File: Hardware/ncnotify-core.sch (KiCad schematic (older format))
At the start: 44 parts, among them J1 BNC5-J-P-GN-RA-BH2D, J2 Conn_ARM_JTAG_SWD_10, J3 USB4110-GF-A, Q1 NX3008NBKS, SW1 SW_Push, SW2 SW_Push, U1 STM32L422CBT6, U2 TLV71333PDBV, U3 USBLC6-2SC6, U4 USBLC6-2SC6, X1 SMTU1632-LF, Y1 Q13FC1350000400

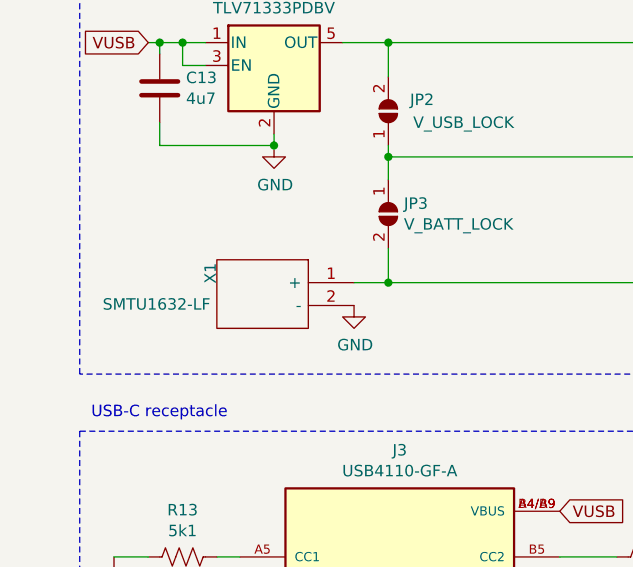
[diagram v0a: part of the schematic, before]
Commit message: sizeup batt to 2032 for current limit; re-place to fit
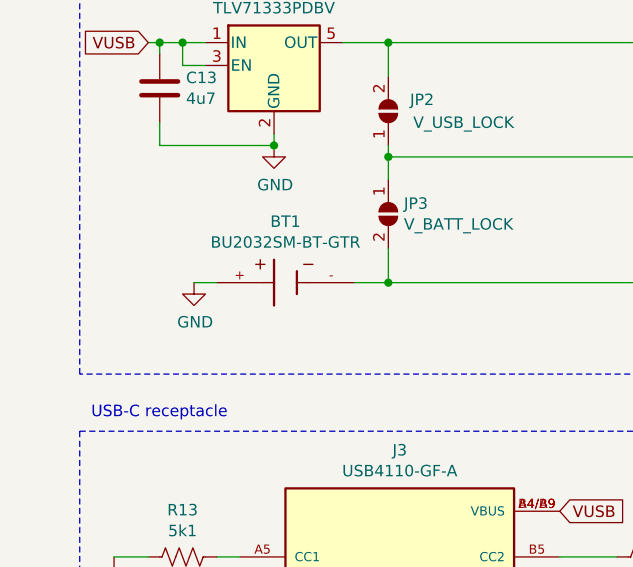
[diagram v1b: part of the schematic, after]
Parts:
- removed X1: SMTU1632-LF, SamacSys_Parts:SMTU1632LF, symbol SamacSys_Parts:SMTU1632-LF
- added BT1: BU2032SM-BT-GTR, BAT_BU2032SM-BT-GTR, symbol BU2032SM-BT-GTR:BU2032SM-BT-GTR
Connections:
- net GND: now also BT1.+
- net VBAT: now also BT1.-
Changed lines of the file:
@@
 Text Notes 3450 600  2    50   ~ 0
 Ext. crystal (LSE)
-$Comp
-L SamacSys_Parts:SMTU1632-LF X1
-U 1 1 5FA9A6FE
-P 1850 5400
-F 0 "X1" V 2478 5396 50  0000 L CNN
-F 1 "SMTU1632-LF" H 2478 5305 50  0000 L CNN
-F 2 "SamacSys_Parts:SMTU1632LF" H 2500 5500 50  0001 L CNN
-F 3 "https://componentsearchengine.com/Datasheets/1/SMTU1632-LF.pdf" H 2500 5400 50  0001 L CNN
-F 4 "Coin Cell Battery Holders SFC MNT FOR CR1632" H 2500 5300 50  0001 L CNN "Description"
-F 5 "5.4" H 2500 5200 50  0001 L CNN "Height"
-F 6 "614-SMTU1632-LF" H 2500 5100 50  0001 L CNN "Mouser Part Number"
-F 7 "https://www.mouser.co.uk/ProductDetail/Renata/SMTU1632-LF?qs=WWgnj3qycfliEHm3l%252BmM0A%3D%3D" H 2500 5000 50  0001 L CNN "Mouser Price/Stock"
-F 8 "RENATA" H 2500 4900 50  0001 L CNN "Manufacturer_Name"
-F 9 "SMTU1632-LF" H 2500 4800 50  0001 L CNN "Manufacturer_Part_Number"
-F 10 "" H 1850 5400 50  0001 C CNN "LCSC Part #"
-	1    1850 5400
-	-1   0    0    -1
-$EndComp
 Text Notes 750  600  0    50   ~ 0
 BNC sense connector
@@
 L power:GND #PWR023
 U 1 1 5FACABCF
-P 1850 5500
-F 0 "#PWR023" H 1850 5250 50  0001 C CNN
-F 1 "GND" H 1855 5327 50  0000 C CNN
-F 2 "" H 1850 5500 50  0001 C CNN
-F 3 "" H 1850 5500 50  0001 C CNN
-	1    1850 5500
+P 1150 5400
+F 0 "#PWR023" H 1150 5150 50  0001 C CNN
+F 1 "GND" H 1155 5227 50  0000 C CNN
+F 2 "" H 1150 5400 50  0001 C CNN
+F 3 "" H 1150 5400 50  0001 C CNN
+	1    1150 5400
 	1    0    0    -1
 $EndComp
@@
 	-1   0    0    1
 $EndComp
+$Comp
+L BU2032SM-BT-GTR:BU2032SM-BT-GTR BT1
+U 1 1 5FDB3DD9
+P 1550 5400
+F 0 "BT1" H 1550 5667 50  0000 C CNN
+F 1 "BU2032SM-BT-GTR" H 1550 5576 50  0000 C CNN
+F 2 "BAT_BU2032SM-BT-GTR" H 1550 5400 50  0001 L BNN
+F 3 "" H 1550 5400 50  0001 L BNN
+F 4 "BU2032SM-HD-G" H 1550 5400 50  0001 L BNN "MP"
+F 5 "MPD _Memory" H 1550 5400 50  0001 L BNN "MF"
+F 6 "None" H 1550 5400 50  0001 L BNN "PACKAGE"
+F 7 "None" H 1550 5400 50  0001 L BNN "PRICE"
+F 8 "F" H 1550 5400 50  0001 L BNN "PARTREV"
+F 9 "5.20mm" H 1550 5400 50  0001 L BNN "MAXIMUM_PACKAGE_HEIGHT"
+F 10 "Unavailable" H 1550 5400 50  0001 L BNN "AVAILABILITY"
+F 11 "BATTERY HOLDER COIN 20MM SMD" H 1550 5400 50  0001 L BNN "DESCRIPTION"
+	1    1550 5400
+	1    0    0    -1
+$EndComp
+Wire Wire Line
+	1150 5400 1250 5400
 $EndSCHEMATC

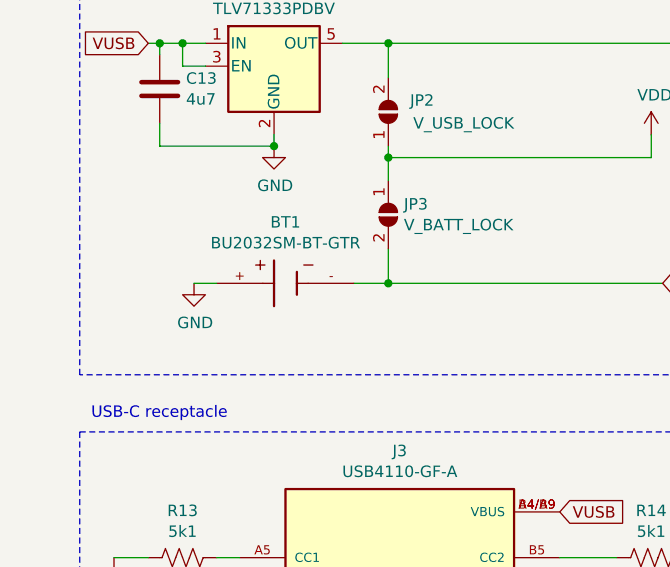
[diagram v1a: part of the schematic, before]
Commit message: Resolve TH conflicts; add 3d models
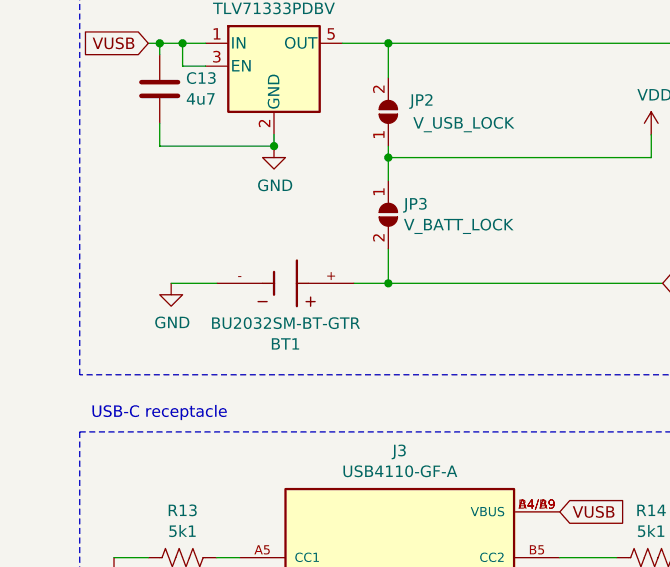
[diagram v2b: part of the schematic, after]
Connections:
- net GND: now also BT1.-; no longer BT1.+
- net VBAT: now also BT1.+; no longer BT1.-
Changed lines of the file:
@@
 L power:GND #PWR023
 U 1 1 5FACABCF
-P 1150 5400
-F 0 "#PWR023" H 1150 5150 50  0001 C CNN
-F 1 "GND" H 1155 5227 50  0000 C CNN
-F 2 "" H 1150 5400 50  0001 C CNN
-F 3 "" H 1150 5400 50  0001 C CNN
-	1    1150 5400
+P 1050 5400
+F 0 "#PWR023" H 1050 5150 50  0001 C CNN
+F 1 "GND" H 1055 5227 50  0000 C CNN
+F 2 "" H 1050 5400 50  0001 C CNN
+F 3 "" H 1050 5400 50  0001 C CNN
+	1    1050 5400
 	1    0    0    -1
 $EndComp
@@
 F 11 "BATTERY HOLDER COIN 20MM SMD" H 1550 5400 50  0001 L BNN "DESCRIPTION"
 	1    1550 5400
-	1    0    0    -1
-$EndComp
-Wire Wire Line
-	1150 5400 1250 5400
+	-1   0    0    1
+$EndComp
+Wire Wire Line
+	1050 5400 1250 5400
 $EndSCHEMATC

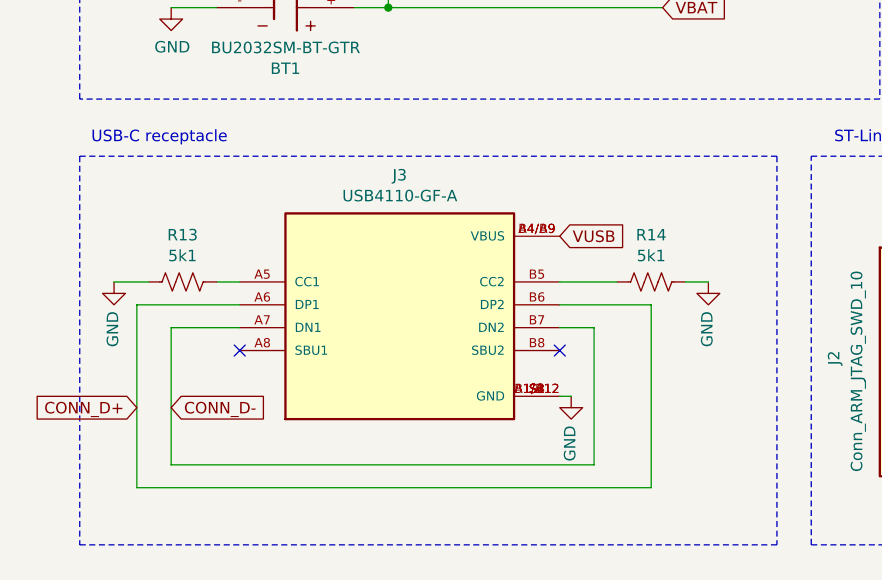
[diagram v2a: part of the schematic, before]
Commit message: micro-usb connector
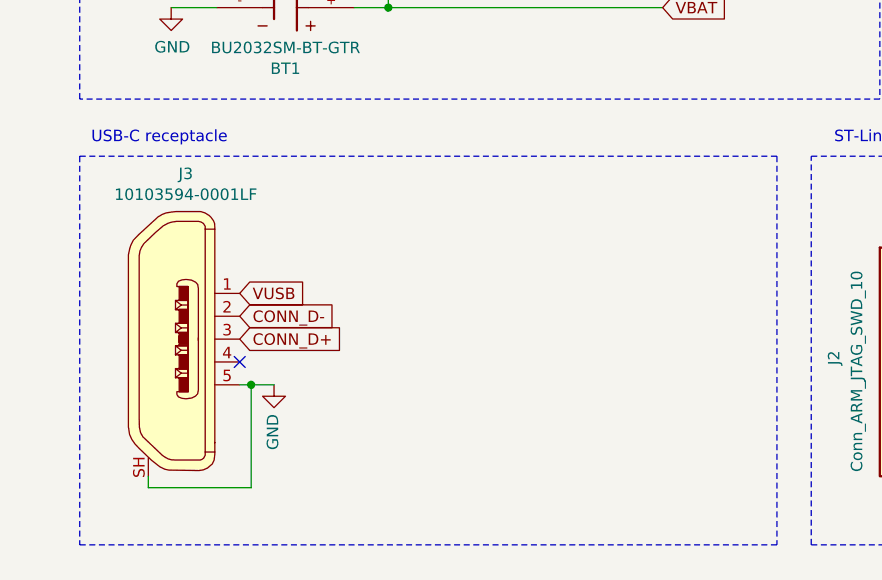
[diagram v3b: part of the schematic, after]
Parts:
- removed J3: USB4110-GF-A, libs:GCT_USB4110-GF-A, symbol USB4110-GF-A:USB4110-GF-A
- removed R13, R14: 5k1, Resistor_SMD:R_0402_1005Metric, symbol Device:R_US
- added J3: 10103594-0001LF, digikey-footprints:USB_Micro_B_Female_10103594-0001LF, symbol dk_USB-DVI-HDMI-Connectors:10103594-0001LF
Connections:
- net CONN_D+: now also J3.3
- net CONN_D-: now also J3.2
- net GND: now also J3.5, J3.SH
- net VUSB: now also J3.1
- no-connect marks 26 -> 25
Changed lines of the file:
@@
 Text Notes 750  600  0    50   ~ 0
 BNC sense connector
-$Comp
-L USB4110-GF-A:USB4110-GF-A J3
-U 1 1 5FA9CA6A
-P 2050 6700
-F 0 "J3" H 2050 7267 50  0000 C CNN
-F 1 "USB4110-GF-A" H 2050 7176 50  0000 C CNN
-F 2 "libs:GCT_USB4110-GF-A" H 2050 6700 50  0001 L BNN
-F 3 "" H 2050 6700 50  0001 L BNN
-F 4 "3.26 mm" H 2050 6700 50  0001 L BNN "MAXIMUM_PACKAGE_HEIGHT"
-F 5 "A" H 2050 6700 50  0001 L BNN "PARTREV"
-F 6 "GCT" H 2050 6700 50  0001 L BNN "MANUFACTURER"
-F 7 "Manufacturer Recommendations" H 2050 6700 50  0001 L BNN "STANDARD"
-F 8 "" H 2050 6700 50  0001 C CNN "LCSC Part #"
-	1    2050 6700
-	1    0    0    -1
-$EndComp
-Text GLabel 900  7150 0    50   Input ~ 0
+Text GLabel 1350 6850 2    50   Input ~ 0
 CONN_D+
-Text GLabel 1050 7150 2    50   Input ~ 0
+Text GLabel 1350 6750 2    50   Input ~ 0
 CONN_D-
-Wire Wire Line
-	1350 6800 1050 6800
-Wire Wire Line
-	1050 7400 2900 7400
-Wire Wire Line
-	900  7500 900  6700
-Wire Wire Line
-	900  6700 1350 6700
-Text GLabel 2750 6400 2    50   Input ~ 0
+Text GLabel 1350 6650 2    50   Input ~ 0
 VUSB
 Wire Notes Line
@@
 Wire Notes Line
 	4950 650  4950 2050
-Wire Wire Line
-	1050 6800 1050 7400
-$Comp
-L Device:R_US R14
-U 1 1 5FAA6CB5
-P 3150 6600
-F 0 "R14" V 2945 6600 50  0000 C CNN
-F 1 "5k1" V 3036 6600 50  0000 C CNN
-F 2 "Resistor_SMD:R_0402_1005Metric" V 3190 6590 50  0001 C CNN
-F 3 "~" H 3150 6600 50  0001 C CNN
-F 4 "C25905" H 3150 6600 50  0001 C CNN "LCSC Part #"
-	1    3150 6600
-	0    1    1    0
-$EndComp
-$Comp
-L Device:R_US R13
-U 1 1 5FAA8706
-P 1100 6600
-F 0 "R13" V 895 6600 50  0000 C CNN
-F 1 "5k1" V 986 6600 50  0000 C CNN
-F 2 "Resistor_SMD:R_0402_1005Metric" V 1140 6590 50  0001 C CNN
-F 3 "~" H 1100 6600 50  0001 C CNN
-F 4 "C25905" H 1100 6600 50  0001 C CNN "LCSC Part #"
-	1    1100 6600
-	0    1    1    0
-$EndComp
-$Comp
-L power:GND #PWR028
-U 1 1 5FAA8F7D
-P 3400 6600
-F 0 "#PWR028" H 3400 6350 50  0001 C CNN
-F 1 "GND" V 3405 6472 50  0000 R CNN
-F 2 "" H 3400 6600 50  0001 C CNN
-F 3 "" H 3400 6600 50  0001 C CNN
-	1    3400 6600
-	-1   0    0    -1
-$EndComp
-$Comp
-L power:GND #PWR027
-U 1 1 5FAA933D
-P 800 6600
-F 0 "#PWR027" H 800 6350 50  0001 C CNN
-F 1 "GND" V 805 6472 50  0000 R CNN
-F 2 "" H 800 6600 50  0001 C CNN
-F 3 "" H 800 6600 50  0001 C CNN
-	1    800  6600
-	-1   0    0    -1
-$EndComp
-Wire Wire Line
-	3400 6600 3300 6600
-Wire Wire Line
-	3000 6600 2750 6600
-Wire Wire Line
-	1350 6600 1250 6600
-Wire Wire Line
-	950  6600 800  6600
 $Comp
 L power:GND #PWR029
 U 1 1 5FAA1030
-P 2800 7100
-F 0 "#PWR029" H 2800 6850 50  0001 C CNN
-F 1 "GND" V 2805 6972 50  0000 R CNN
-F 2 "" H 2800 7100 50  0001 C CNN
-F 3 "" H 2800 7100 50  0001 C CNN
-	1    2800 7100
+P 1500 7050
+F 0 "#PWR029" H 1500 6800 50  0001 C CNN
+F 1 "GND" V 1505 6922 50  0000 R CNN
+F 2 "" H 1500 7050 50  0001 C CNN
+F 3 "" H 1500 7050 50  0001 C CNN
+	1    1500 7050
 	-1   0    0    -1
 $EndComp
-NoConn ~ 2750 6900
-NoConn ~ 1350 6900
 $Comp
 L Regulator_Linear:TLV71333PDBV U2
@@
 Wire Notes Line
 	5300 5600 5300 4150
-Wire Wire Line
-	2900 6800 2750 6800
 Wire Notes Line
 	650  7750 3700 7750
@@
 Wire Notes Line
 	650  6050 650  7750
-Wire Wire Line
-	3150 6700 3150 7500
-Wire Wire Line
-	2900 6800 2900 7400
-Wire Wire Line
-	2750 6700 3150 6700
-Wire Wire Line
-	900  7500 3150 7500
 Text GLabel 5850 3050 2    50   Input ~ 0
 D+
@@
 Connection ~ 1500 4800
 Wire Wire Line
-	2800 7100 2750 7100
-Wire Wire Line
 	900  3500 900  3450
 Wire Wire Line
@@
 Wire Wire Line
 	1050 5400 1250 5400
+Wire Wire Line
+	1350 7050 1400 7050
+NoConn ~ 1350 6950
+Connection ~ 1400 7050
+Wire Wire Line
+	1400 7050 1500 7050
+Wire Wire Line
+	950  7450 950  7500
+Wire Wire Line
+	950  7500 1400 7500
+Wire Wire Line
+	1400 7050 1400 7500
+$Comp
+L dk_USB-DVI-HDMI-Connectors:10103594-0001LF J3
+U 1 1 5FF142B1
+P 1100 6850
+F 0 "J3" H 1114 7573 50  0000 C CNN
+F 1 "10103594-0001LF" H 1114 7482 50  0000 C CNN
+F 2 "digikey-footprints:USB_Micro_B_Female_10103594-0001LF" H 1300 7050 60  0001 L CNN
+F 3 "https://cdn.amphenol-icc.com/media/wysiwyg/files/drawing/10103594.pdf" H 1300 7150 60  0001 L CNN
+F 4 "609-4050-1-ND" H 1300 7250 60  0001 L CNN "Digi-Key_PN"
+F 5 "10103594-0001LF" H 1300 7350 60  0001 L CNN "MPN"
+F 6 "Connectors, Interconnects" H 1300 7450 60  0001 L CNN "Category"
+F 7 "USB, DVI, HDMI Connectors" H 1300 7550 60  0001 L CNN "Family"
+F 8 "https://cdn.amphenol-icc.com/media/wysiwyg/files/drawing/10103594.pdf" H 1300 7650 60  0001 L CNN "DK_Datasheet_Link"
+F 9 "/product-detail/en/amphenol-icc-fci/10103594-0001LF/609-4050-1-ND/2350357" H 1300 7750 60  0001 L CNN "DK_Detail_Page"
+F 10 "CONN RCPT USB2.0 MICRO B SMD R/A" H 1300 7850 60  0001 L CNN "Description"
+F 11 "Amphenol ICC (FCI)" H 1300 7950 60  0001 L CNN "Manufacturer"
+F 12 "Active" H 1300 8050 60  0001 L CNN "Status"
+	1    1100 6850
+	1    0    0    -1
+$EndComp
 $EndSCHEMATC
